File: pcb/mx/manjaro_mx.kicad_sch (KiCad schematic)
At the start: 99 parts, among them SW1 SW_Push, SW10 SW_Push, SW11 SW_Push, SW12 SW_Push, SW13 SW_Push, SW14 SW_Push, SW15 SW_Push, SW16 SW_Push, SW17 SW_Push, SW18 SW_Push, SW19 SW_Push, SW2 SW_Push, SW20 SW_Push, SW21 SW_Push, SW22 SW_Push, SW23 SW_Push, SW24 SW_Push, SW3 SW_Push, SW4 SW_Push, SW5 SW_Push, SW6 SW_Push, SW7 SW_Push, SW8 SW_Push, SW9 SW_Push, U1 nice_nano

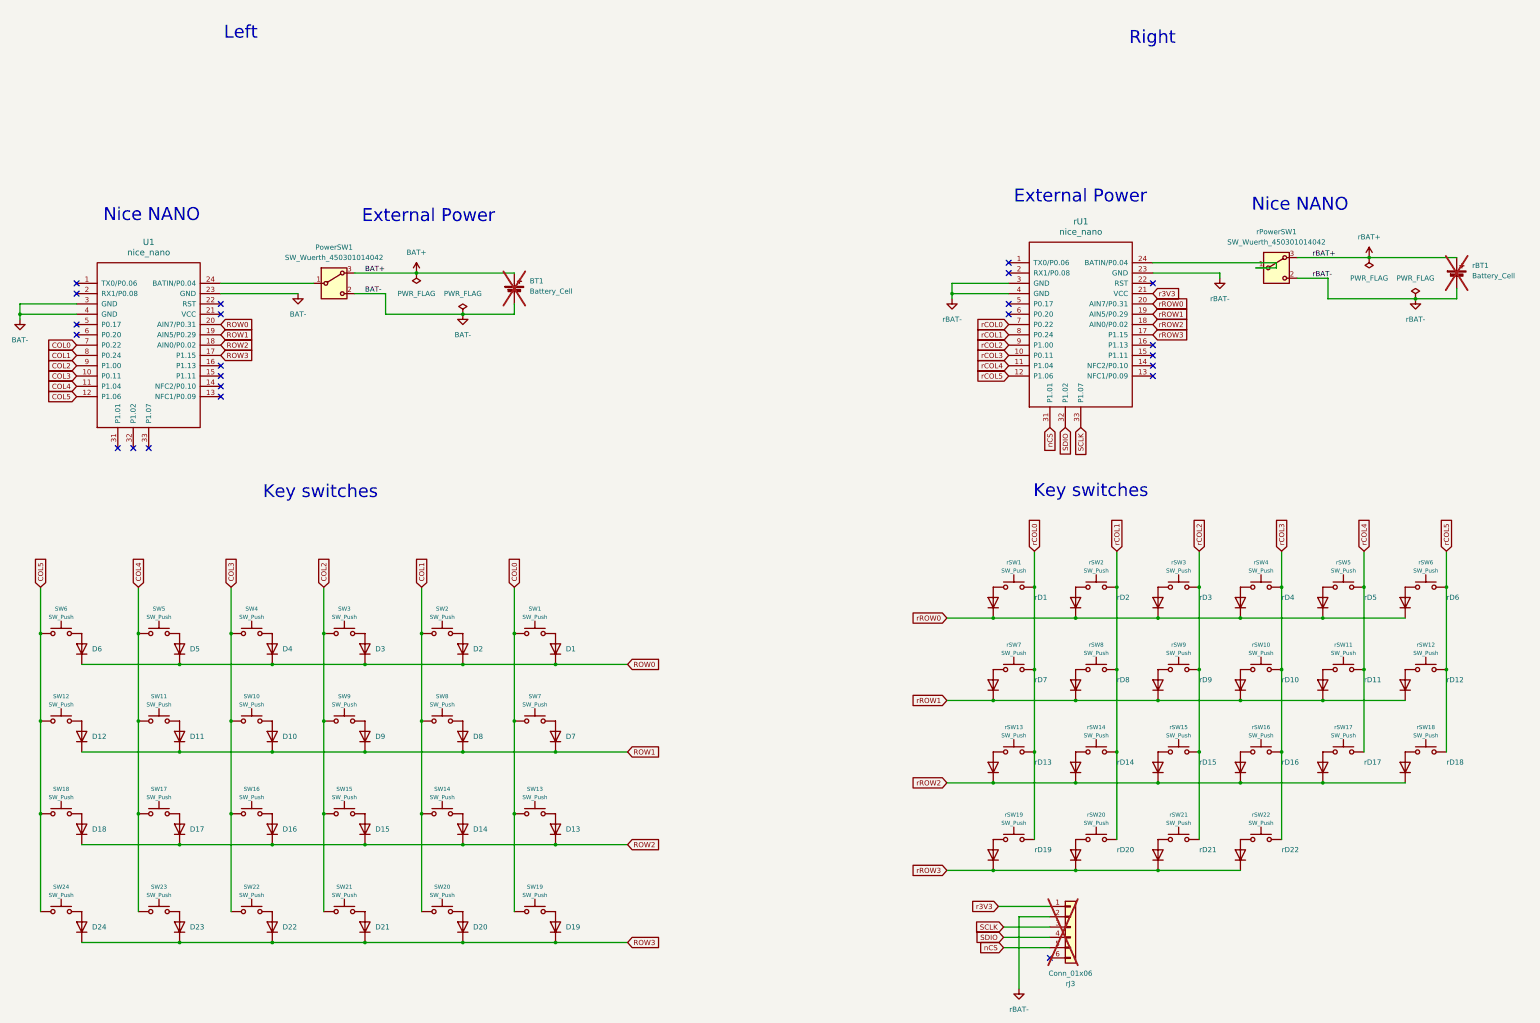
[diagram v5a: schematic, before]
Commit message: fixed keylayout & MCU position
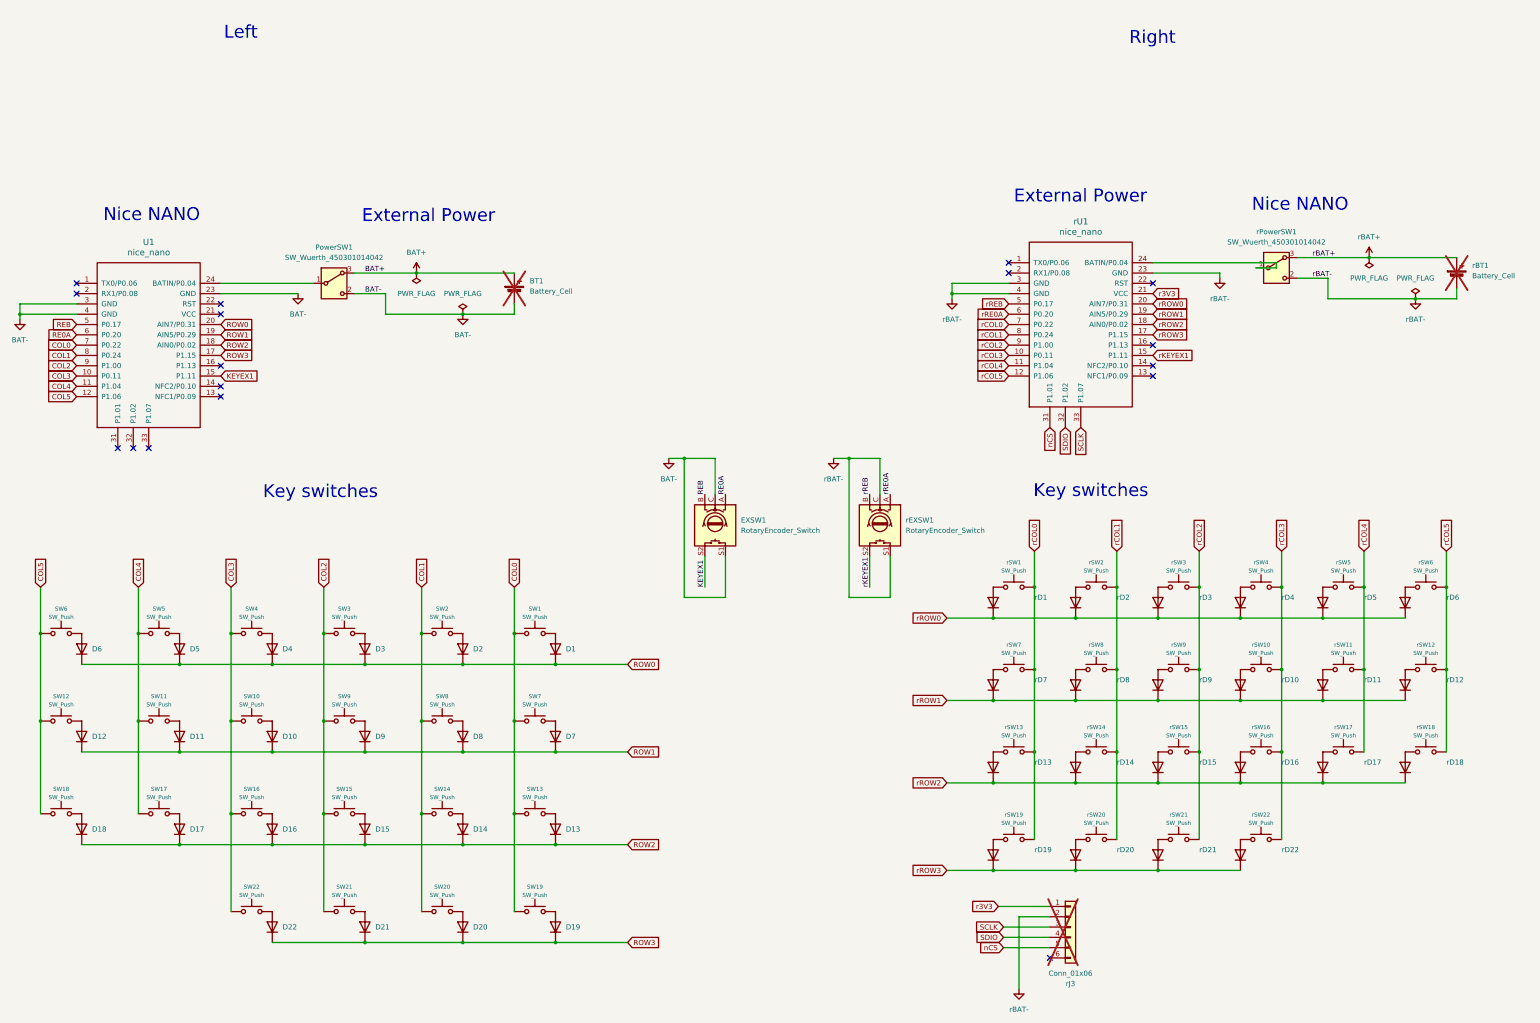
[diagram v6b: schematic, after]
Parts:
- removed D23, D24: 1N4148WT, Keebio-Parts:D_SOD-323, symbol Diode:1N4148WT
- removed SW23, SW24: SW_Push, kbd_SW:Choc_Hotswap_1u, symbol Switch:SW_Push
- added EXSW1, rEXSW1: RotaryEncoder_Switch, Keebio-Parts:RotaryEncoder_EC11, symbol Device:RotaryEncoder_Switch
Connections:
- net BAT-: now also EXSW1.C, EXSW1.S1
- net rBAT-: now also rEXSW1.C, rEXSW1.S1
- net rKEYEX1: now reaches rU1.15 (P1.11)
- net rKEYEX1: now also rEXSW1.S2
- net rREB: now reaches rU1.5 (P0.17)
- net rREB: now also rEXSW1.B
- net rRE0A: now reaches rU1.6 (P0.20)
- net rRE0A: now also rEXSW1.A
- net KEYEX1: now reaches U1.15 (P1.11)
- net KEYEX1: now also EXSW1.S2
- net REB: now reaches U1.5 (P0.17)
- net REB: now also EXSW1.B
- net RE0A: now reaches U1.6 (P0.20)
- net RE0A: now also EXSW1.A
- no-connect marks 23 -> 17

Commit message: Fixed v1 layout
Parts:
- removed rD22: 1N4148WT, Keebio-Parts:D_SOD-323, symbol Diode:1N4148WT
- removed rSW22: SW_Push, kbd_SW:Choc_Hotswap_1u, symbol Switch:SW_Push
- added D23: 1N4148WT, Keebio-Parts:D_SOD-323, symbol Diode:1N4148WT
- added J1, rJ1: AudioJack3, kbd:PJ-398A-5A_PJ-399B-6A, symbol Connector_Audio:AudioJack3
- added J2, rJ2: MJ-4PP-9, MJ-4PP-9:MJ-4PP-9, symbol MJ-4PP-9:MJ-4PP-9
- added SW23: SW_Push, kbd:keyswitch_cherrymx_hotswap_1u, symbol Switch:SW_Push
- SW1, SW10, SW11, SW12, SW13, SW14, SW15, SW16, SW17, SW18, SW19, SW2, SW20, SW21, SW22, SW3, SW4, SW5, SW6, SW7, SW8, SW9, rSW1, rSW10, rSW11, rSW12, rSW13, rSW14, rSW15, rSW16, rSW17, rSW18, rSW19, rSW2, rSW20, rSW21, rSW3, rSW4, rSW5, rSW6, rSW7, rSW8, rSW9: footprint kbd_SW:Choc_Hotswap_1u -> kbd:keyswitch_cherrymx_hotswap_1u
- rJ3: now fitted
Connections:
- net BAT-: now also J1.S, J2.3 (C)
- net COL4: now also SW23.1
- net KEYEX1: now also U1.1 (TX0/P0.06); no longer U1.15 (P1.11)
- net ROW3: now also D23.1 (K)
- net SCLK: now also rU1.16 (P1.13); no longer rU1.33 (P1.07)
- net SDIO: now also rU1.15 (P1.11); no longer rU1.32 (P1.02)
- net rBAT-: now also rJ1.S, rJ2.3 (C)
- net rKEYEX1: now also rU1.1 (TX0/P0.06); no longer rU1.15 (P1.11)
- net NCS: now reaches rU1.13 (NFC1/P0.09)
- net NCS: now also rJ3.5 (Pin_5)
- net rDATA: now reaches rU1.2 (RX1/P0.08)
- net rDATA: now also rJ1.R, rJ2.2 (B)
- net DATA: now reaches U1.2 (RX1/P0.08)
- net DATA: now also J1.R, J2.2 (B)
- net VCC: now reaches U1.21 (VCC)
- net VCC: now also J1.T, J2.4 (D)
- net nCS: no longer names the net of rU1.31 (P1.01)
- net nCS: no longer rJ3.5 (Pin_5)
- net r3V3 renamed rVCC
- net rVCC: now also rJ1.T, rJ2.4 (D)
- new net: D23.2 (A), SW23.2
- no-connect marks 17 -> 16
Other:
- moved on the sheet: BT1, D1, D10, D11, D12, D13, D14, D15, D16, D17, D18, D19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

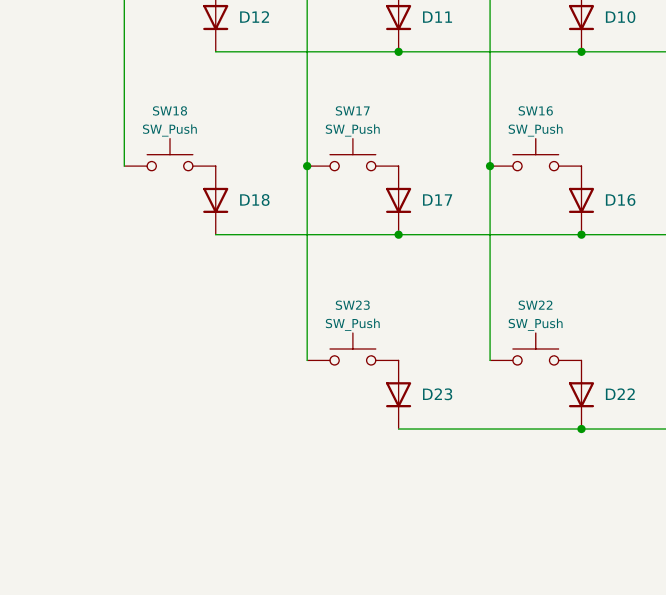
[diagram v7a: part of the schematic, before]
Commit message: Add 1key on left hand
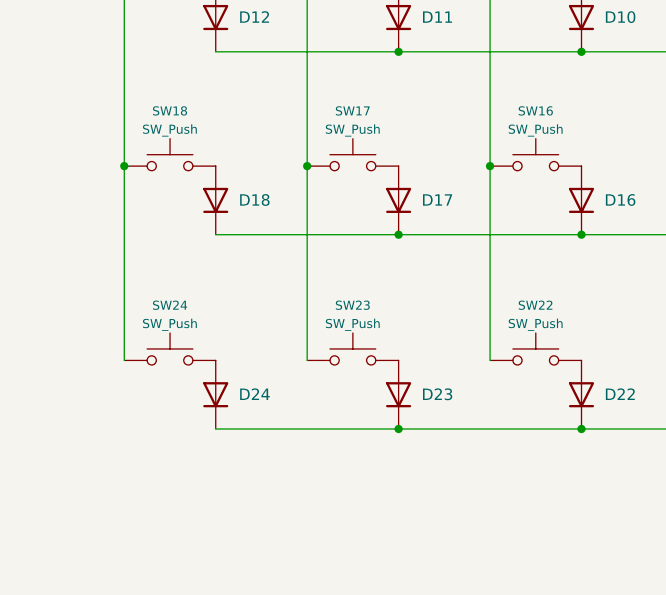
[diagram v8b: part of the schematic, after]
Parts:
- added D24: 1N4148WT, Keebio-Parts:D_SOD-323, symbol Diode:1N4148WT
- added SW24: SW_Push, kbd:keyswitch_cherrymx_hotswap_1u, symbol Switch:SW_Push
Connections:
- net COL5: now also SW24.1
- net ROW3: now also D24.1 (K)
- new net: D24.2 (A), SW24.2
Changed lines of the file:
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@@
 	)
 	(junction
+		(at 39.37 209.55)
+		(diameter 0)
+		(color 0 0 0 0)
+	)
+	(junction
 		(at 130.81 176.53)
 		(diameter 0)
@@
 	)
 	(junction
+		(at 69.85 238.76)
+		(diameter 0)
+		(color 0 0 0 0)
+	)
+	(junction
 		(at 140.97 189.23)
 		(diameter 0)
@@
 	(wire
 		(pts
+			(xy 39.37 209.55) (xy 39.37 231.14)
+		)
+		(stroke
+			(width 0)
+			(type default)
+		)
+	)
+	(wire
+		(pts
 			(xy 231.14 238.76) (xy 242.57 238.76)
 		)
@@
 	(wire
 		(pts
+			(xy 49.53 238.76) (xy 69.85 238.76)
+		)
+		(stroke
+			(width 0)
+			(type default)
+		)
+	)
+	(wire
+		(pts
 			(xy 151.13 196.85) (xy 168.91 196.85)
 		)
@@
 	)
 	(symbol
+		(lib_id "Diode:1N4148WT")
+		(at 49.53 234.95 90)
+		(unit 1)
+		(exclude_from_sim no)
+		(in_bom yes)
+		(on_board yes)
+		(dnp no)
+		(fields_autoplaced yes)
+		(property "Reference" "D24"
+			(at 52.07 234.9499 90)
+			(effects
+				(font
+					(size 1.27 1.27)
+				)
+				(justify right)
+			)
+		)
+		(property "Value" "1N4148WT"
+			(at 52.07 236.2199 90)
+			(effects
+				(font
+					(size 1.27 1.27)
+				)
+				(justify right)
+				(hide yes)
+			)
+		)
+		(property "Footprint" "Keebio-Parts:D_SOD-323"
+			(at 53.975 234.95 0)
+			(effects
+				(font
+					(size 1.27 1.27)
+				)
+				(hide yes)
+			)
+		)
+		(property "Datasheet" "https://www.diodes.com/assets/Datasheets/ds30396.pdf"
+			(at 49.53 234.95 0)
+			(effects
+				(font
+					(size 1.27 1.27)
+				)
+				(hide yes)
+			)
+		)
+		(property "Description" "75V 0.15A Fast switching Diode, SOD-523"
+			(at 49.53 234.95 0)
+			(effects
+				(font
+					(size 1.27 1.27)
+				)
+				(hide yes)
+			)
+		)
+		(property "Sim.Device" "D"
+			(at 49.53 234.95 0)
+			(effects
+				(font
+					(size 1.27 1.27)
+				)
+				(hide yes)
+			)
+		)
+		(property "Sim.Pins" "1=K 2=A"
+			(at 49.53 234.95 0)
+			(effects
+				(font
+					(size 1.27 1.27)
+				)
+				(hide yes)
+			)
+		)
+		(pin "1"
+		)
+		(pin "2"
+		)
+		(instances
+			(project "manjaro_mx"
+				(path "/d6bc4a6e-b820-400a-83ff-ae45032fef21"
+					(reference "D24")
+					(unit 1)
+				)
+			)
+		)
+	)
+	(symbol
 		(lib_id "MJ-4PP-9:MJ-4PP-9")
 		(at 317.5 116.84 0)
@@
 					(unit 1)
 				)
+			)
+		)
+	)
+	(symbol
+		(lib_id "Switch:SW_Push")
+		(at 44.45 231.14 0)
+		(unit 1)
+		(exclude_from_sim no)
+		(in_bom yes)
+		(on_board yes)
+		(dnp no)
+		(property "Reference" "SW24"
+			(at 44.45 225.044 0)
+			(effects
+				(font
+					(size 1 1)
+				)
+			)
+		)
+		(property "Value" "SW_Push"
+			(at 44.45 227.076 0)
+			(effects
+				(font
+					(size 1 1)
+				)
+			)
+		)
+		(property "Footprint" "kbd:keyswitch_cherrymx_hotswap_1u"
+			(at 44.45 226.06 0)
+			(effects
+				(font
+					(size 1.27 1.27)
+				)
+				(hide yes)
+			)
+		)
+		(property "Datasheet" "~"
+			(at 44.45 226.06 0)
+			(effects
+				(font
+					(size 1.27 1.27)
+				)
+				(hide yes)
+			)
+		)
+		(property "Description" ""
+			(at 44.45 231.14 0)
+			(effects
+				(font
+					(size 1.27 1.27)
+				)
+				(hide yes)
+			)
+		)
+		(pin "1"
+		)
+		(pin "2"
+		)
+		(instances
+			(project "manjaro_mx"
+				(path "/d6bc4a6e-b820-400a-83ff-ae45032fef21"
+					(reference "SW24")
+					(unit 1)
+				)
